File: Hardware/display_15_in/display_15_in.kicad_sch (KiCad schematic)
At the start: 2 parts, among them J1 559592430, U9 S16B-PHDSSLFSN

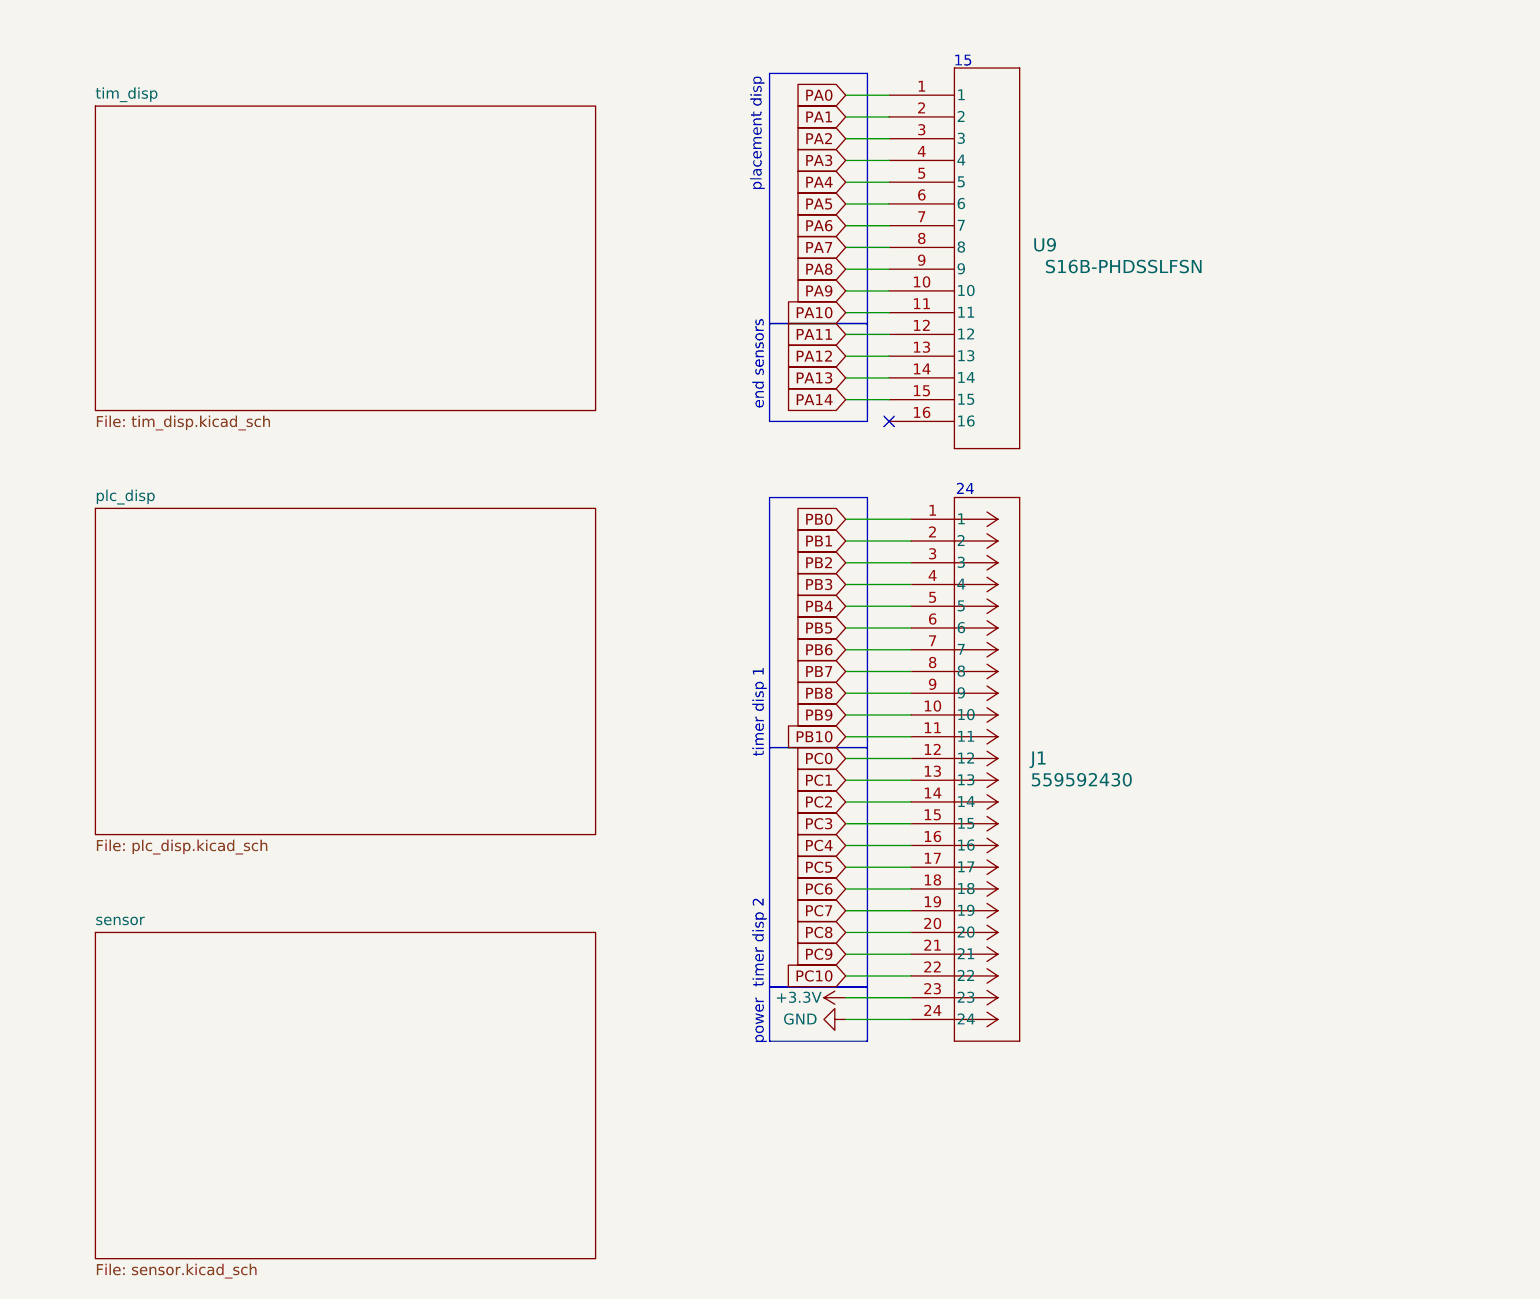
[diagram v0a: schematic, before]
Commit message: routed more traces
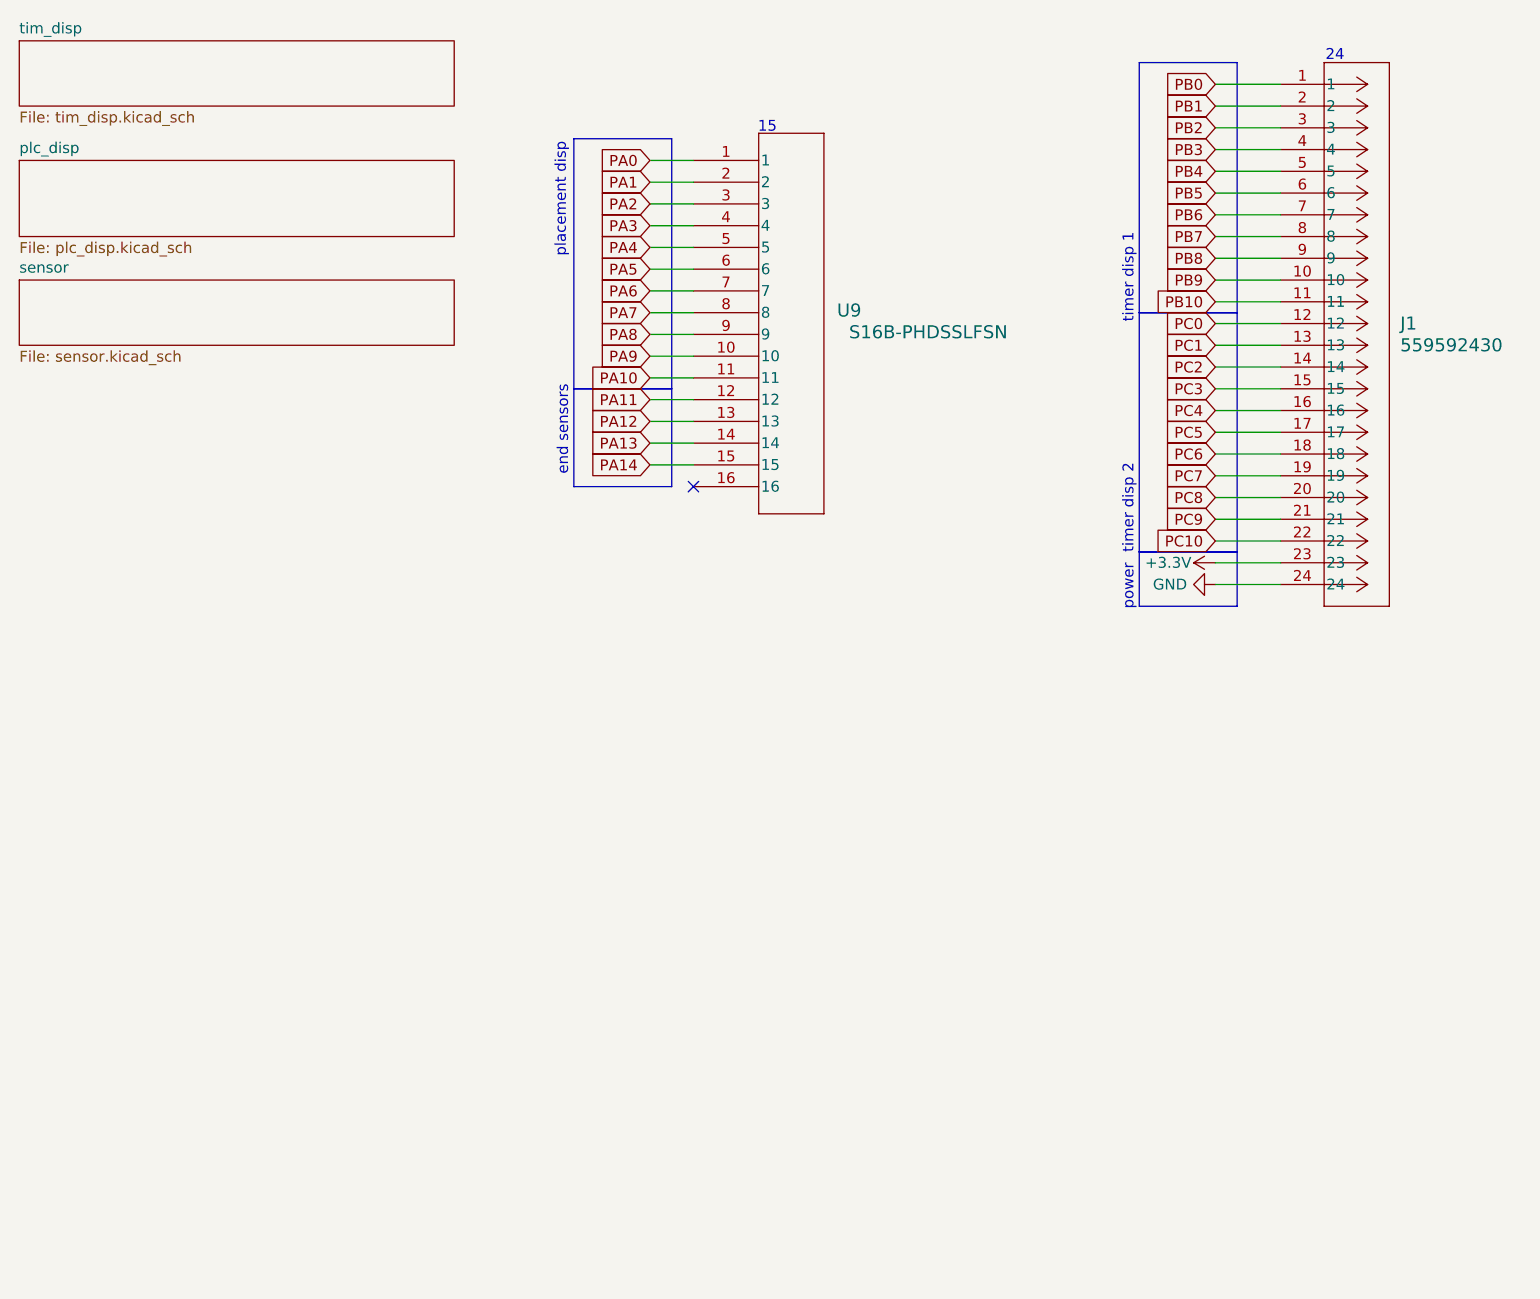
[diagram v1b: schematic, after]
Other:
- moved on the sheet: J1, U9

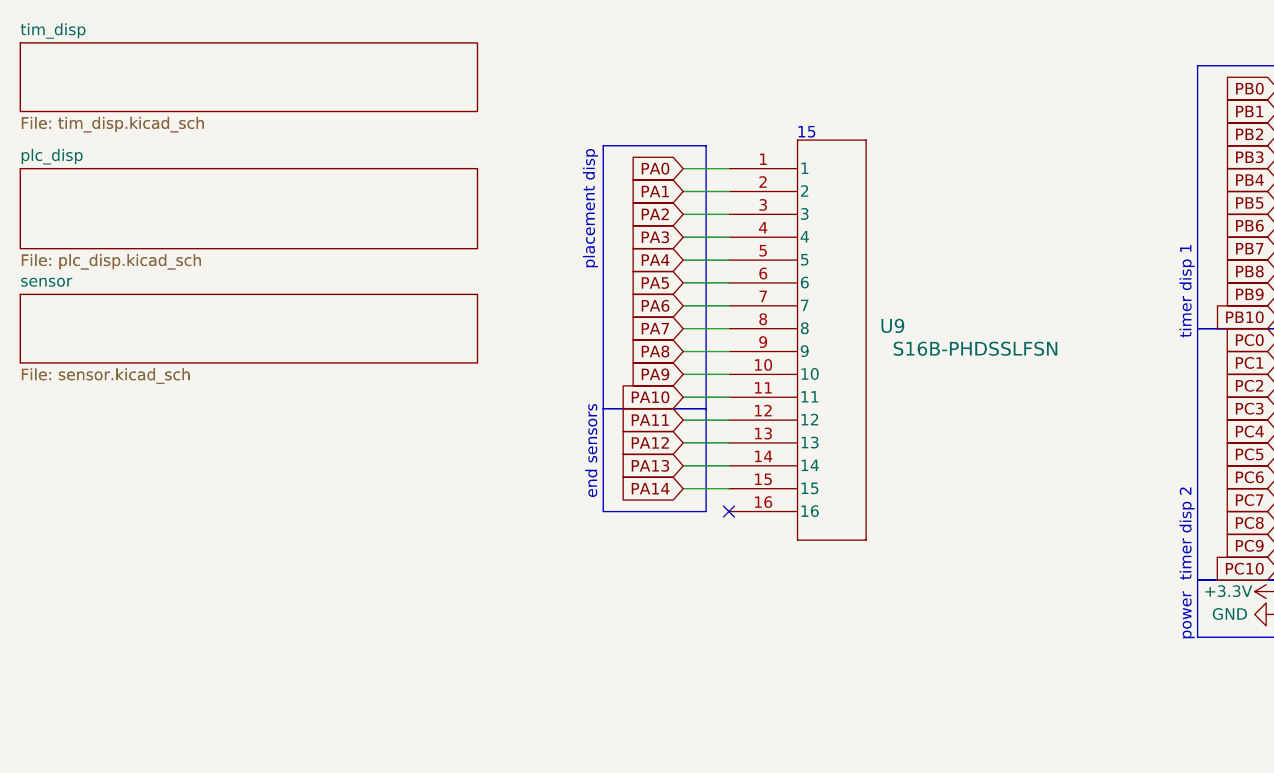
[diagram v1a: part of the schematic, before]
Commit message: power traces, gnd plane vias, and test points
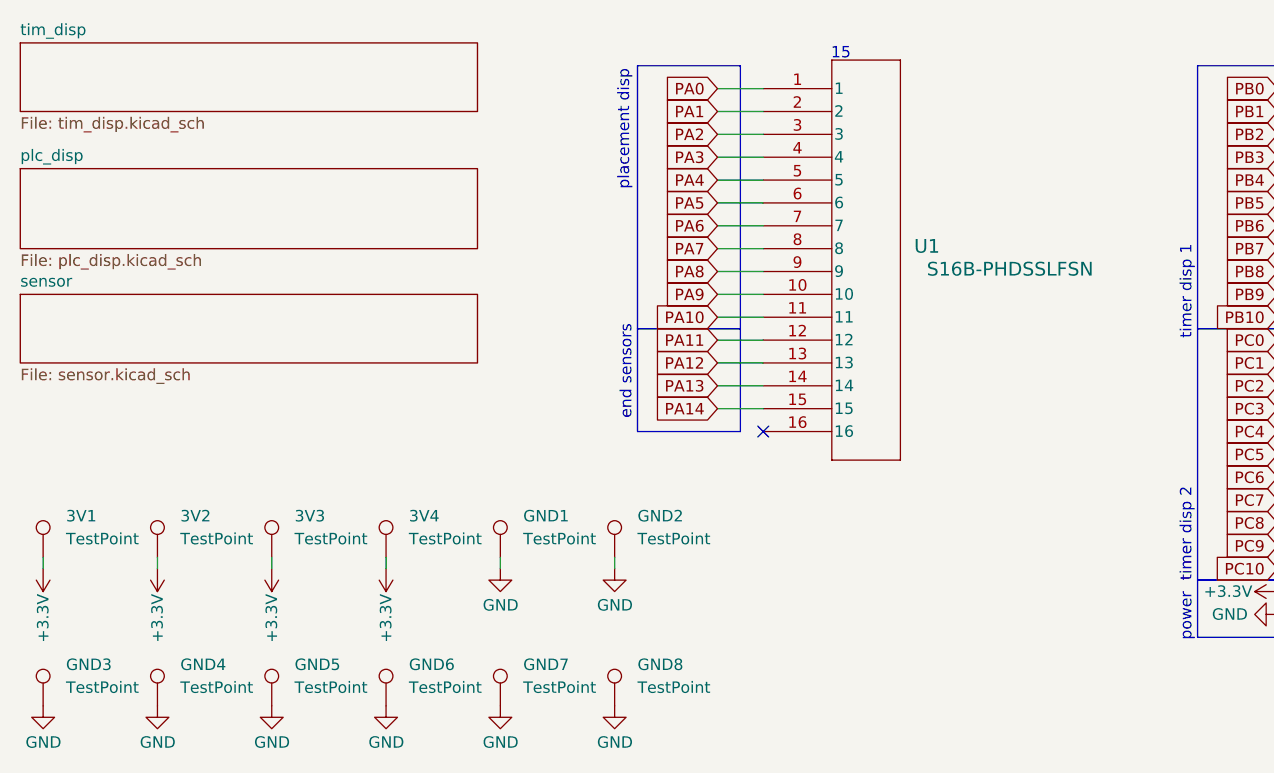
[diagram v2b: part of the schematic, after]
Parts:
- added 3V1, 3V2, 3V3, 3V4, GND1, GND2, GND3, GND4, GND5, GND6, GND7, GND8: TestPoint, TestPoint:TestPoint_Keystone_5019_Minature, symbol Connector:TestPoint
- renumbered U9 to U1
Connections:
- net +3.3V: now also 3V1.1, 3V2.1, 3V3.1, 3V4.1
- net GND: now also GND1.1, GND2.1, GND3.1, GND4.1, GND5.1, GND6.1, GND7.1, GND8.1
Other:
- moved on the sheet: U1

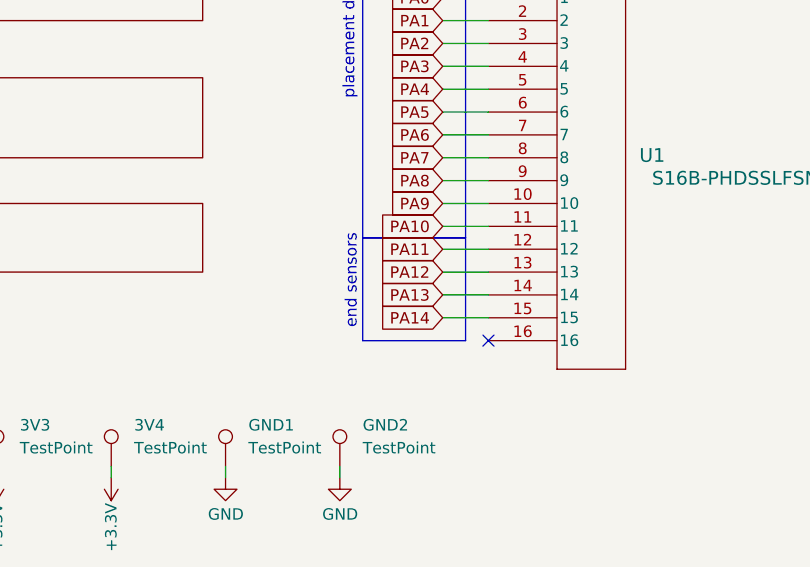
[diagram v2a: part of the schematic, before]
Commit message: began work on mainboard
mostly schematic but i did assign footprints (if you even consider that to be working on the pcb)
power in from usb and ONLY power from usb - no dp just vbus and gnd. still dnt know what cc or shield is but i can figure that out later
jtag and usb-ttl for programming. will not be powered by usb while programmed.
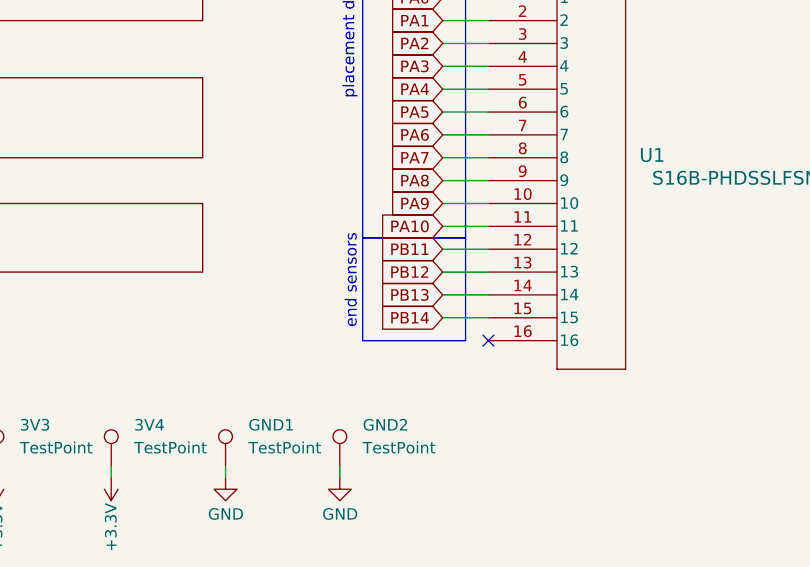
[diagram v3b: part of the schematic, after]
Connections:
- net PA11 renamed PB11
- net PA12 renamed PB12
- net PA13 renamed PB13
- net PA14 renamed PB14
